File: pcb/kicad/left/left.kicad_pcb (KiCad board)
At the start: 2 copper layers, 135.9 x 89.9 mm, 61 parts, among them J1 USB_C_Receptacle_USB2.0, J2 AudioJack4, J3 Conn_01x12_Male, SW1 BOOT, SW10 SW_Push, SW12 SW_Push, SW13 SW_Push, SW14 SW_Push, SW15 SW_Push, SW17 SW_Push, SW18 SW_Push, SW19 SW_Push, SW2 RESET, SW21 SW_Push, SW22 SW_Push, SW23 SW_Push, SW24 SW_Push, SW3 SW_Push, SW31 SW_Push, SW32 SW_Push, SW33 SW_Push, SW34 SW_Push, SW4 SW_Push, SW5 SW_Push, SW7 SW_Push, SW8 SW_Push, SW9 SW_Push, U1 STM32, U2 LDO

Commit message: Corrections on the PCB
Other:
- board size 135.9 x 89.9 mm -> 135.9 x 89.5 mm
- board text added: "KeySeeBee v0.3 by TeXitoi"
- board text removed: "KeySeeBee v0.2 by TeXitoi"
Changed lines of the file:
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@@
       (drillshape 0)
       (scaleselection 1)
-      (outputdirectory "../../gerbers/v0.2/left/"))
+      (outputdirectory "../../gerbers/v0.3/left/"))
   )
   (net 0 "")
@@
     (effects (font (size 0.8 0.8) (thickness 0.2)))
   )
-  (gr_text "KeySeeBee v0.2 by TeXitoi" (at 238.633 104.775 90) (layer F.SilkS)
+  (gr_text "KeySeeBee v0.3 by TeXitoi" (at 238.76 104.14 90) (layer F.SilkS)
     (effects (font (size 1 1) (thickness 0.2)) (justify left))
   )
@@
   (gr_line (start 152.4 120.65) (end 104.775 114.3) (layer Edge.Cuts) (width 0.1))
   (gr_line (start 190.5 123.19) (end 152.4 120.65) (layer Edge.Cuts) (width 0.1))
-  (gr_line (start 227.203 131.826) (end 190.5 123.19) (layer Edge.Cuts) (width 0.1))
-  (gr_line (start 240.665 104.775) (end 227.203 131.826) (layer Edge.Cuts) (width 0.1))
-  (gr_line (start 240.665 46.99) (end 240.665 104.775) (layer Edge.Cuts) (width 0.1))
+  (gr_line (start 226.822 131.445) (end 190.5 123.19) (layer Edge.Cuts) (width 0.1))
+  (gr_line (start 240.665 104.14) (end 226.822 131.445) (layer Edge.Cuts) (width 0.1))
+  (gr_line (start 240.665 46.99) (end 240.665 104.14) (layer Edge.Cuts) (width 0.1))
   (gr_line (start 219.075 46.99) (end 240.665 46.99) (layer Edge.Cuts) (width 0.1))
   (gr_line (start 180.975 41.91) (end 219.075 46.99) (layer Edge.Cuts) (width 0.1))

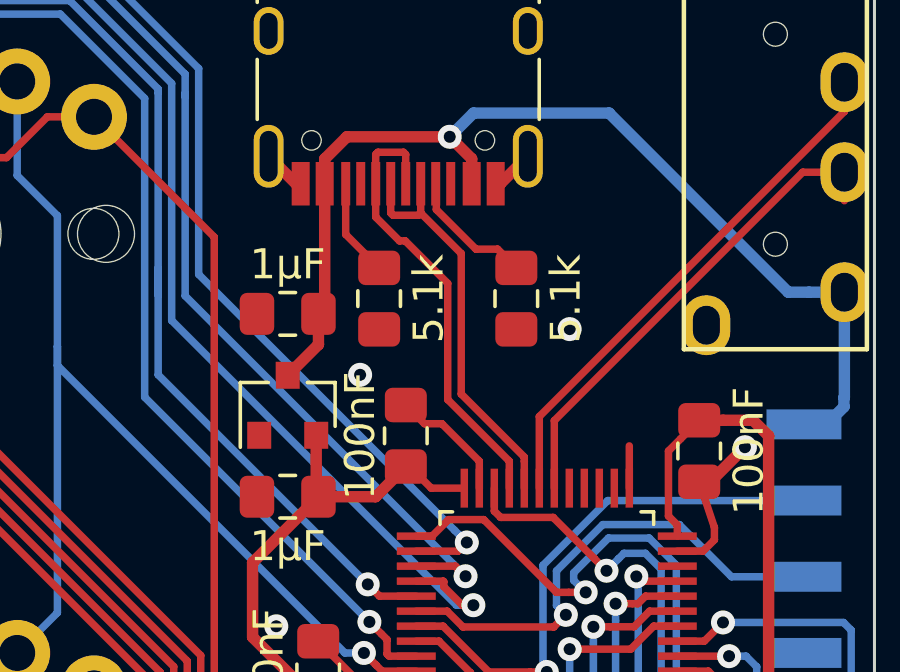
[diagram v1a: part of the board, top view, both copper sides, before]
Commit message: More parallel usb trace on left
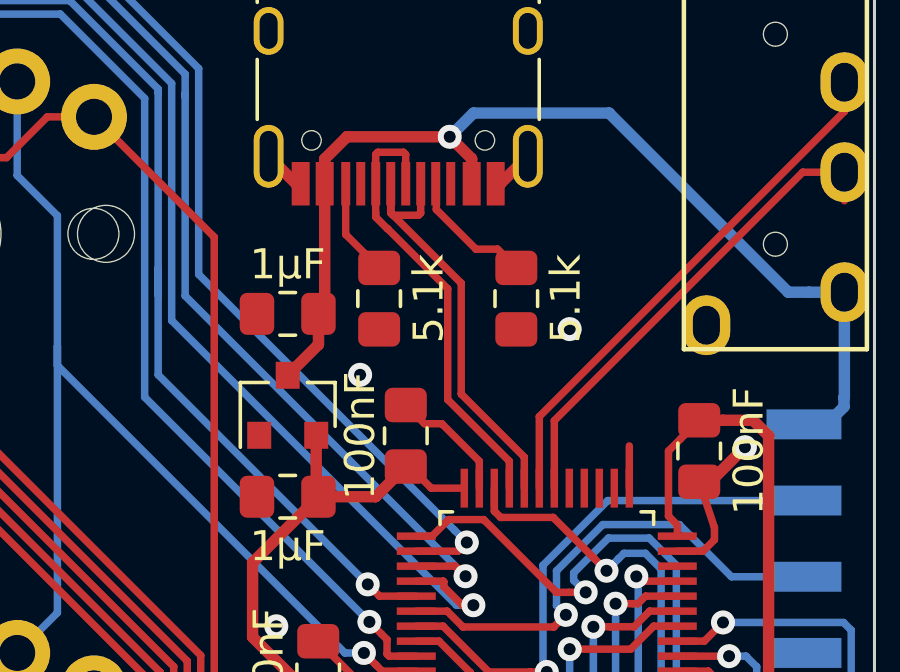
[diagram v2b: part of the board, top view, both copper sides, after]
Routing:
- net D-: track 13.6 -> 15.0 mm
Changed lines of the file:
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@@
     (thickness 1.6)
     (drawings 25)
-    (tracks 718)
+    (tracks 719)
     (zones 0)
     (modules 61)
@@
   (segment (start 225.54 55.82) (end 225.54 54.845) (width 0.25) (layer F.Cu) (net 5))
   (segment (start 224.54 54.845) (end 224.54 55.82) (width 0.25) (layer F.Cu) (net 5))
-  (segment (start 228.993 64.092) (end 228.993 64.992) (width 0.25) (layer F.Cu) (net 5))
-  (segment (start 228.993 63.95559) (end 228.993 64.092) (width 0.25) (layer F.Cu) (net 5))
-  (segment (start 226.89101 61.8536) (end 228.993 63.95559) (width 0.25) (layer F.Cu) (net 5))
-  (segment (start 226.89101 57.17101) (end 226.89101 61.8536) (width 0.25) (layer F.Cu) (net 5))
-  (segment (start 225.54 55.82) (end 226.89101 57.17101) (width 0.25) (layer F.Cu) (net 5))
+  (segment (start 226.89101 58.16041) (end 224.54 55.8094) (width 0.25) (layer F.Cu) (net 5))
+  (segment (start 226.89101 61.8536) (end 226.89101 58.16041) (width 0.25) (layer F.Cu) (net 5))
+  (segment (start 228.993 63.95559) (end 226.89101 61.8536) (width 0.25) (layer F.Cu) (net 5))
+  (segment (start 224.54 55.8094) (end 224.54 54.845) (width 0.25) (layer F.Cu) (net 5))
+  (segment (start 228.993 64.992) (end 228.993 63.95559) (width 0.25) (layer F.Cu) (net 5))
   (segment (start 225.04 53.87) (end 225.04 54.845) (width 0.25) (layer F.Cu) (net 6))
   (segment (start 224.964999 53.794999) (end 225.04 53.87) (width 0.25) (layer F.Cu) (net 6))
@@
   (segment (start 224.04 53.87) (end 224.115001 53.794999) (width 0.25) (layer F.Cu) (net 6))
   (segment (start 224.04 54.845) (end 224.04 53.87) (width 0.25) (layer F.Cu) (net 6))
-  (segment (start 228.493 64.092) (end 228.493 64.992) (width 0.25) (layer F.Cu) (net 6))
-  (segment (start 224.04 55.95641) (end 224.83258 56.74899) (width 0.25) (layer F.Cu) (net 6))
-  (segment (start 224.04 54.845) (end 224.04 55.95641) (width 0.25) (layer F.Cu) (net 6))
-  (segment (start 224.83258 56.74899) (end 225.02399 56.74899) (width 0.25) (layer F.Cu) (net 6))
-  (segment (start 225.02399 56.74899) (end 226.441 58.166) (width 0.25) (layer F.Cu) (net 6))
-  (segment (start 226.441 58.166) (end 226.441 62.04) (width 0.25) (layer F.Cu) (net 6))
-  (segment (start 226.441 62.04) (end 228.493 64.092) (width 0.25) (layer F.Cu) (net 6))
+  (segment (start 224.04 55.82) (end 224.04 54.845) (width 0.25) (layer F.Cu) (net 6))
+  (segment (start 224.04 55.95641) (end 224.04 55.82) (width 0.25) (layer F.Cu) (net 6))
+  (segment (start 228.493 64.092) (end 226.440999 62.039999) (width 0.25) (layer F.Cu) (net 6))
+  (segment (start 226.440999 62.039999) (end 226.440999 58.346809) (width 0.25) (layer F.Cu) (net 6))
+  (segment (start 226.440999 58.346809) (end 224.439201 56.345011) (width 0.25) (layer F.Cu) (net 6))
+  (segment (start 228.493 64.992) (end 228.493 64.092) (width 0.25) (layer F.Cu) (net 6))
+  (segment (start 224.439201 56.345011) (end 224.4286 56.34501) (width 0.25) (layer F.Cu) (net 6))
+  (segment (start 224.4286 56.34501) (end 224.04 55.95641) (width 0.25) (layer F.Cu) (net 6))
   (segment (start 223.04 56.534) (end 224.155 57.649) (width 0.25) (layer F.Cu) (net 8))
   (segment (start 223.04 54.845) (end 223.04 56.534) (width 0.25) (layer F.Cu) (net 8))

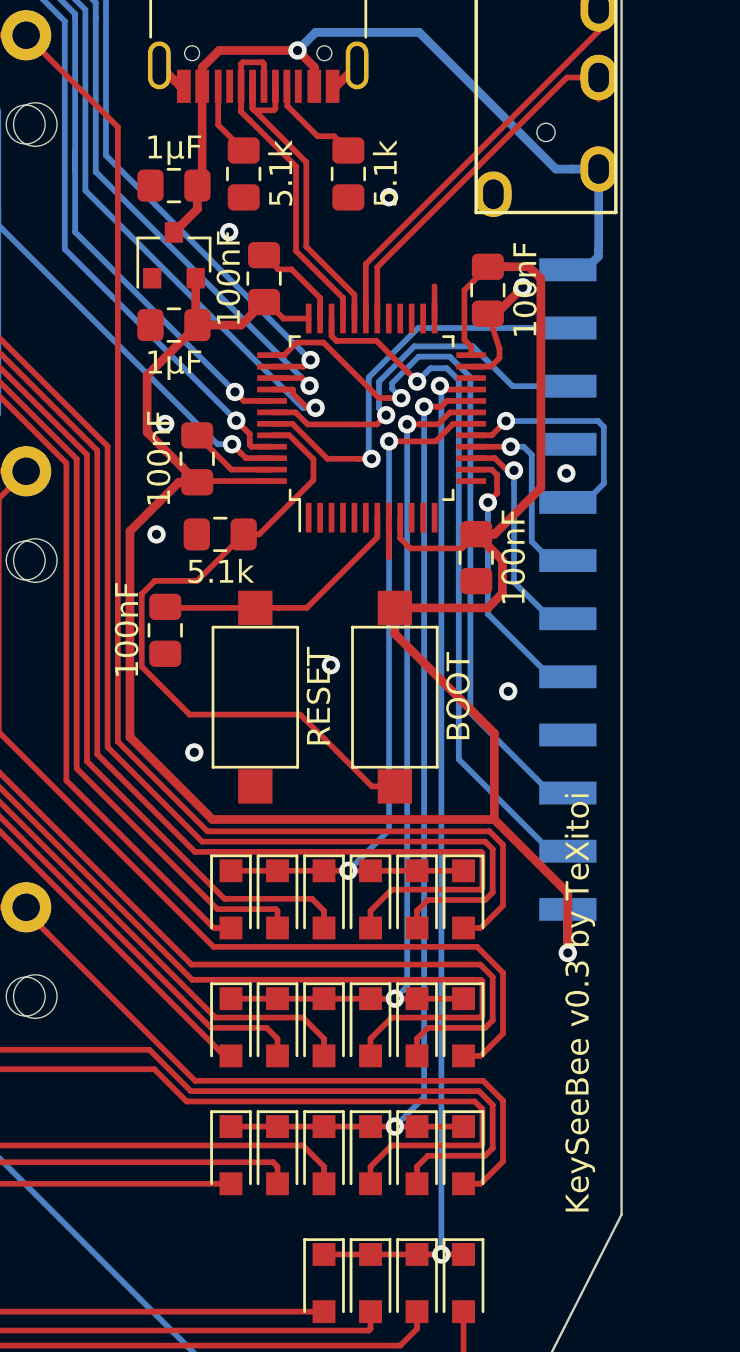
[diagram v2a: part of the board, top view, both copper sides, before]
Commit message: Some try at STM assembly (clearly not yet ready)
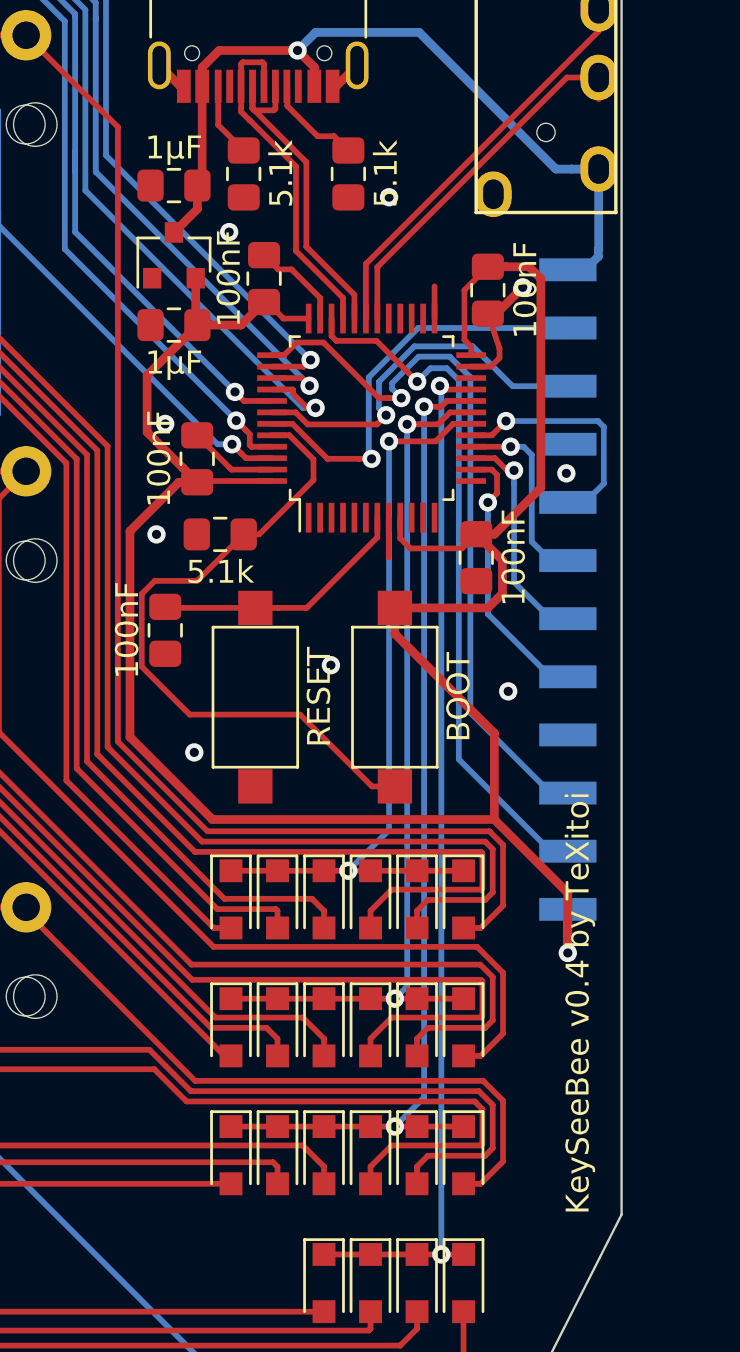
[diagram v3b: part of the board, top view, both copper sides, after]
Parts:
- D10: value D2.3 -> 1N4148WS
- D11: value D3.3 -> 1N4148WS
- D12: value D4.3 -> 1N4148WS
- D14: value D1.6 -> 1N4148WS
- D15: value D2.6 -> 1N4148WS
- D16: value D3.6 -> 1N4148WS
- D17: value D4.6 -> 1N4148WS
- D19: value D1.2 -> 1N4148WS
- D20: value D2.2 -> 1N4148WS
- D21: value D3.2 -> 1N4148WS
- D23: value D1.4 -> 1N4148WS
- D24: value D2.4 -> 1N4148WS
- D25: value D3.4 -> 1N4148WS
- D26: value D4.4 -> 1N4148WS
- D33: value D1.5 -> 1N4148WS
- D34: value D2.5 -> 1N4148WS
- D35: value D3.5 -> 1N4148WS
- D36: value D4.5 -> 1N4148WS
- D5: value D1.1 -> 1N4148WS
- D6: value D2.1 -> 1N4148WS
- D7: value D3.1 -> 1N4148WS
- D9: value D1.3 -> 1N4148WS
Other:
- board text added: "KeySeeBee v0.4 by TeXitoi"
- board text removed: "KeySeeBee v0.3 by TeXitoi"

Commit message: jlcpcb smt and kicad 6
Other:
- net class Default removed

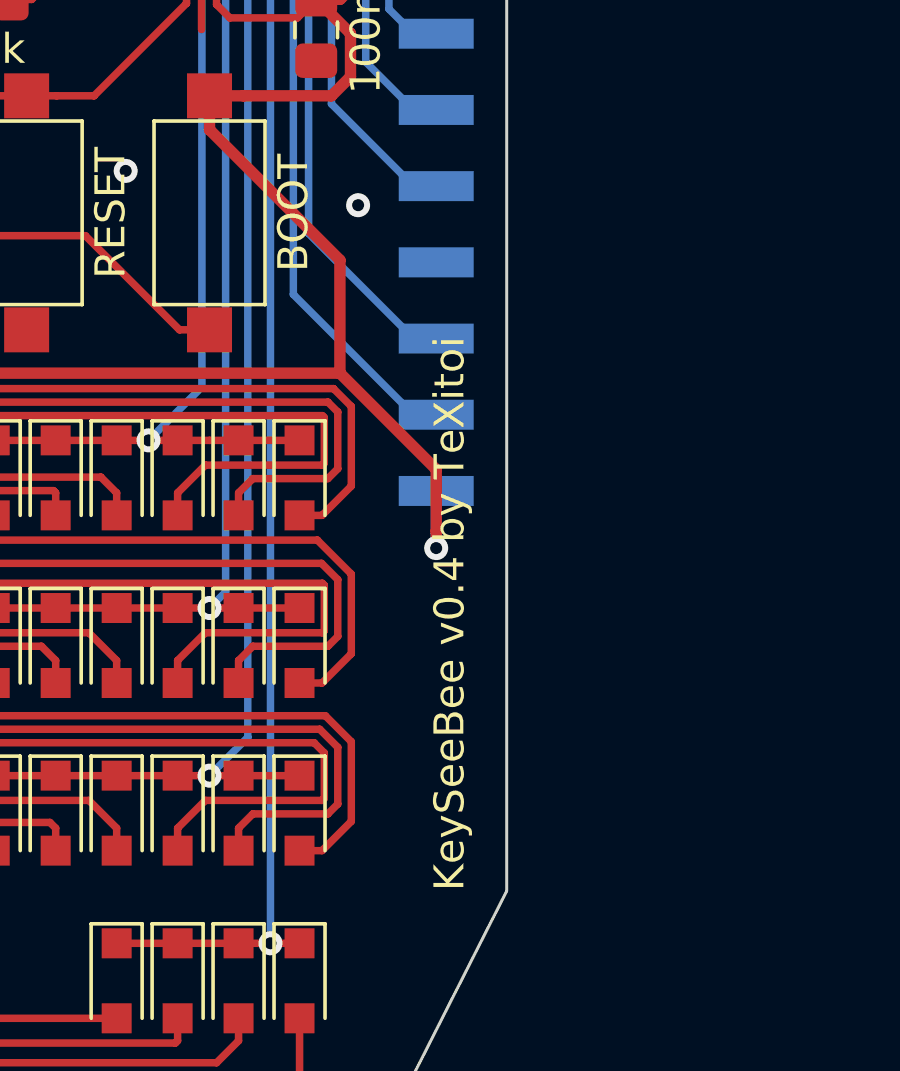
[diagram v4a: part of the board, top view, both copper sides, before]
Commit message: More JLCPCB SMT changes
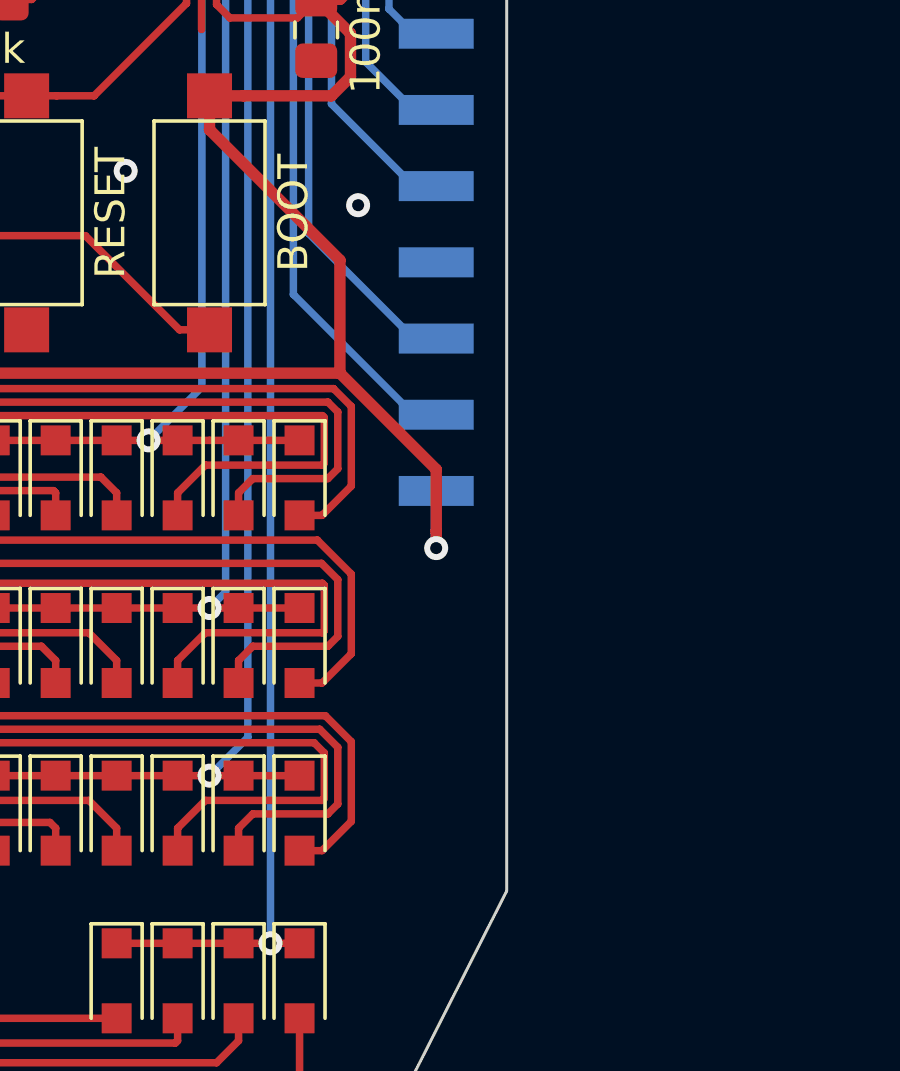
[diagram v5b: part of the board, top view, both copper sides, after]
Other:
- board text removed: "KeySeeBee v0.4 by TeXitoi"
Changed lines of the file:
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@@
     (effects (font (size 0.8 0.8) (thickness 0.2)))
-  )
-  (gr_text "KeySeeBee v0.4 by TeXitoi" (at 238.76 104.14 90) (layer "F.SilkS")
-    (effects (font (size 1 1) (thickness 0.2)) (justify left))
   )
   (segment (start 235.331 66.302999) (end 234.823 64.779) (width 0.25) (layer "F.Cu") (net 1))
